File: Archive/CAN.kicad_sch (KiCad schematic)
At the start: 18 parts, among them U3 ISO1044BD, U4 UCC12050DVE

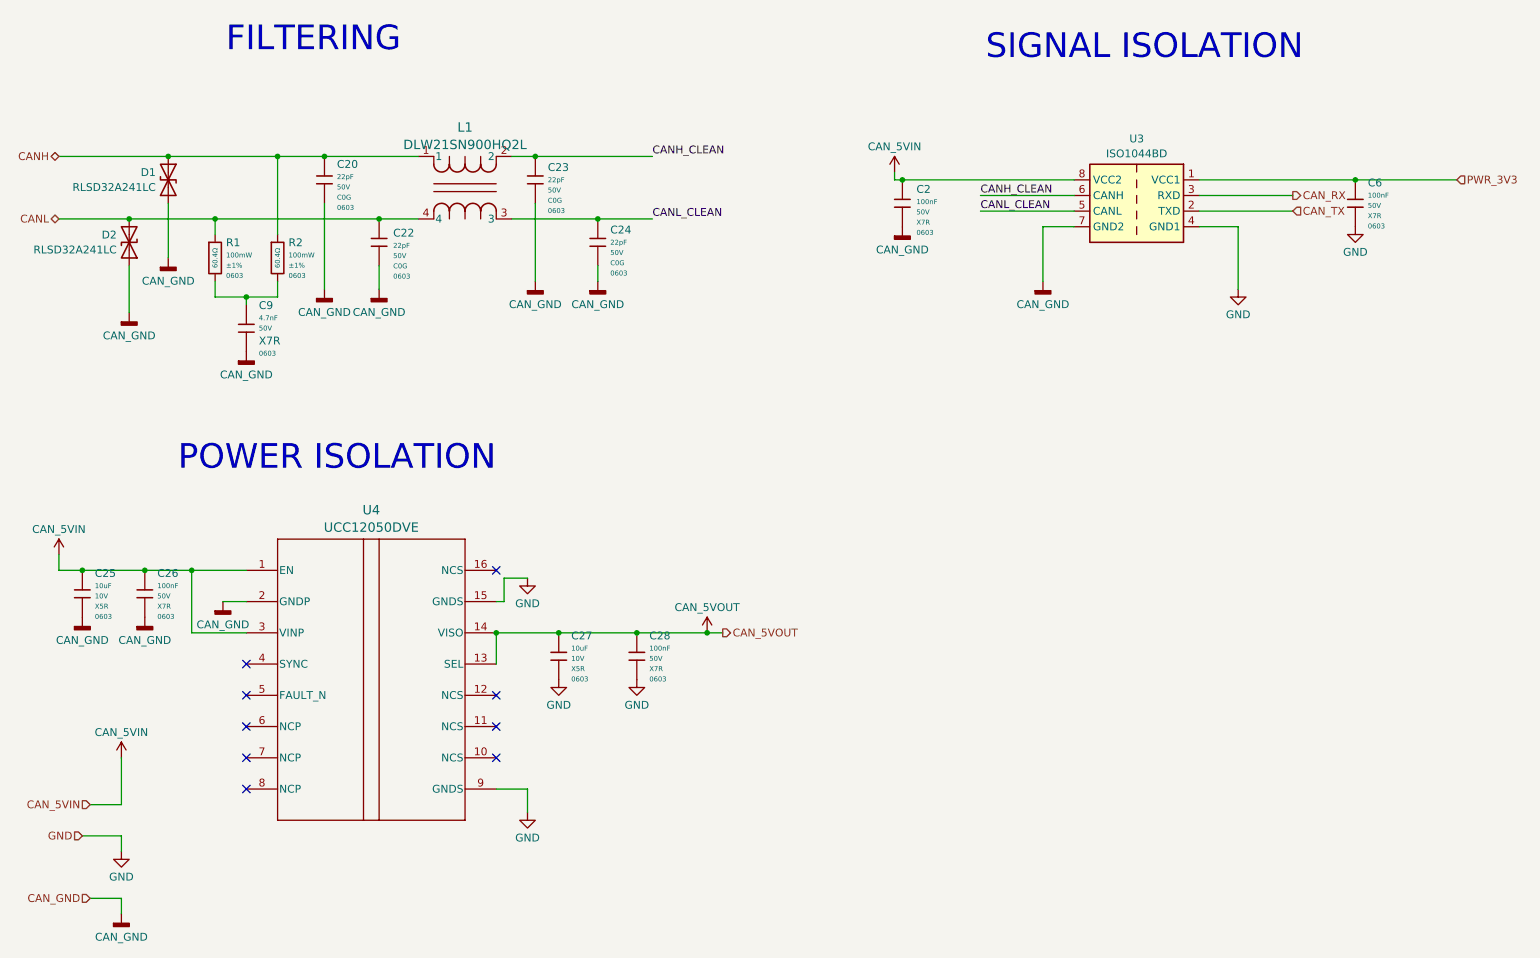
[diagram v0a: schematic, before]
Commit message: Switched to Altium, completed and ordered design
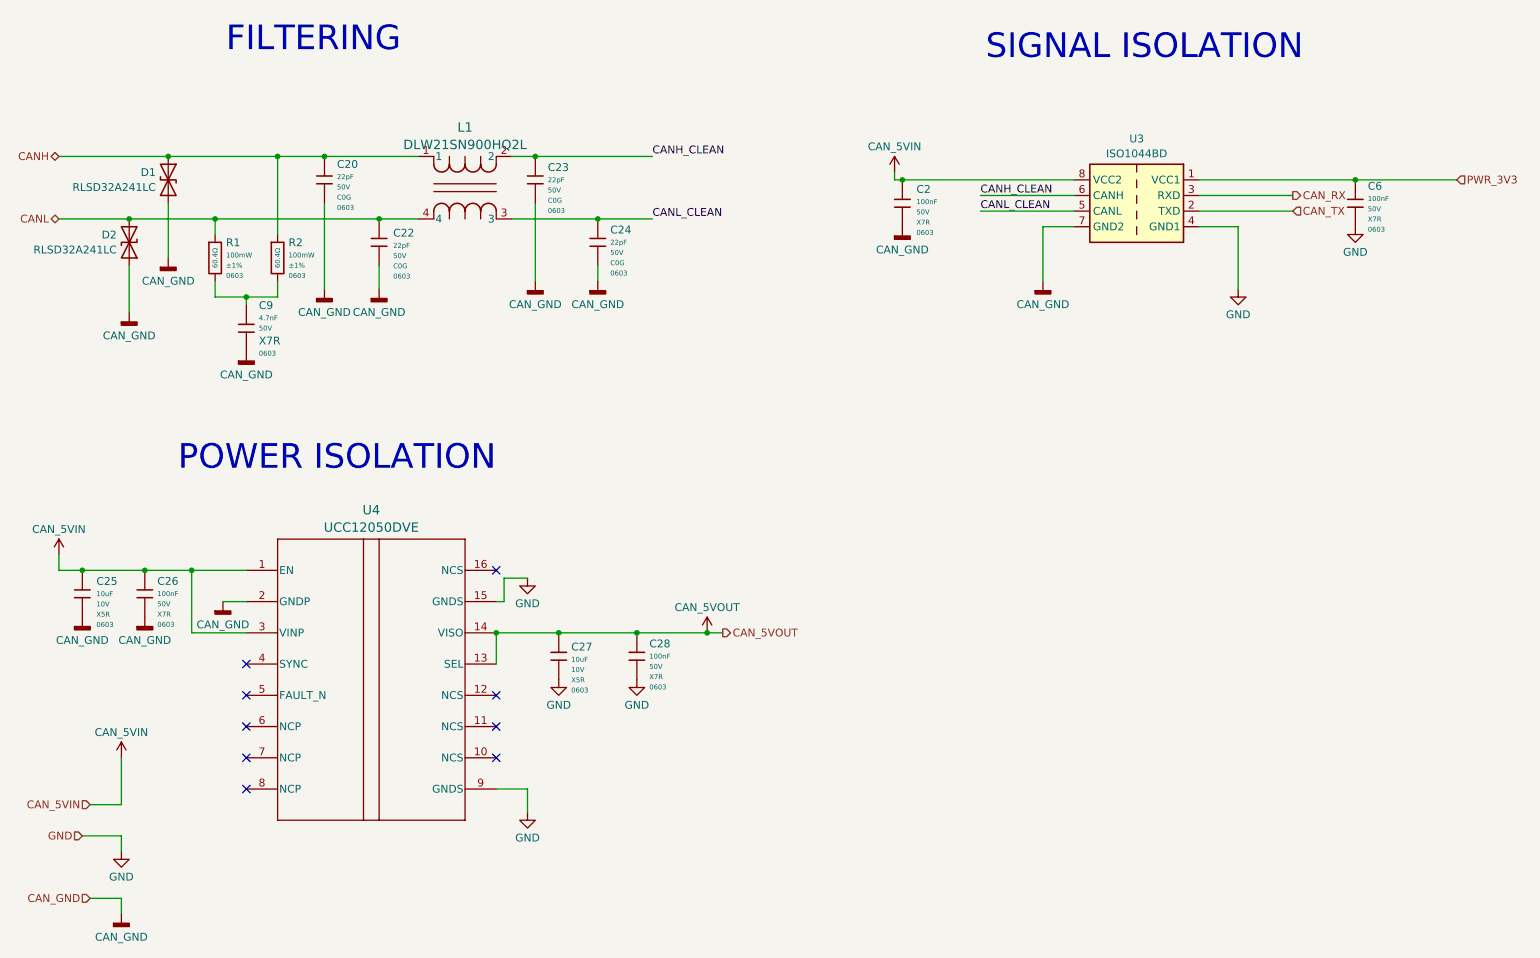
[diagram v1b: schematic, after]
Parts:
- D1, D2: footprint (none) -> PCM_JLCPCB:D_SOD-323
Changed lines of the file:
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@@
 		(on_board yes)
 		(dnp no)
-		(fields_autoplaced yes)
 		(property "Reference" "C25"
-			(at 47.752 127.474 0)
+			(at 48.006 128.778 0)
 			(effects
 				(font
@@
 		)
 		(property "Value" "10uF"
-			(at 47.752 129.5202 0)
+			(at 48.006 130.8242 0)
 			(effects
 				(font
@@
 		)
 		(property "Voltage Rated" "10V"
-			(at 47.752 131.1882 0)
+			(at 48.006 132.4922 0)
 			(effects
 				(font
@@
 		)
 		(property "Temperature Coefficient" "X5R"
-			(at 47.752 132.8562 0)
+			(at 48.006 134.1602 0)
 			(effects
 				(font
@@
 		)
 		(property "Package" "0603"
-			(at 47.752 134.5242 0)
+			(at 48.006 135.8282 0)
 			(effects
 				(font
@@
 		(on_board yes)
 		(dnp no)
-		(fields_autoplaced yes)
 		(property "Reference" "C28"
-			(at 137.922 137.634 0)
+			(at 137.922 138.938 0)
 			(effects
 				(font
@@
 		)
 		(property "Value" "100nF"
-			(at 137.922 139.6802 0)
+			(at 137.922 140.9842 0)
 			(effects
 				(font
@@
 		)
 		(property "Voltage Rated" "50V"
-			(at 137.922 141.3482 0)
+			(at 137.922 142.6522 0)
 			(effects
 				(font
@@
 		)
 		(property "Temperature Coefficient" "X7R"
-			(at 137.922 143.0162 0)
+			(at 137.922 144.3202 0)
 			(effects
 				(font
@@
 		)
 		(property "Package" "0603"
-			(at 137.922 144.6842 0)
+			(at 137.922 145.9882 0)
 			(effects
 				(font
@@
 			)
 		)
-		(property "Footprint" ""
+		(property "Footprint" "PCM_JLCPCB:D_SOD-323"
 			(at 59.69 63.5 0)
 			(effects
@@
 		(on_board yes)
 		(dnp no)
-		(fields_autoplaced yes)
 		(property "Reference" "C6"
-			(at 254.762 63.974 0)
+			(at 254.762 64.516 0)
 			(effects
 				(font
@@
 		)
 		(property "Value" "100nF"
-			(at 254.762 66.0202 0)
+			(at 254.762 66.5622 0)
 			(effects
 				(font
@@
 		)
 		(property "Voltage Rated" "50V"
-			(at 254.762 67.6882 0)
+			(at 254.762 68.2302 0)
 			(effects
 				(font
@@
 		)
 		(property "Temperature Coefficient" "X7R"
-			(at 254.762 69.3562 0)
+			(at 254.762 69.8982 0)
 			(effects
 				(font
@@
 		)
 		(property "Package" "0603"
-			(at 254.762 71.0242 0)
+			(at 254.762 71.5662 0)
 			(effects
 				(font
@@
 		(on_board yes)
 		(dnp no)
-		(fields_autoplaced yes)
 		(property "Reference" "C26"
-			(at 57.912 127.474 0)
+			(at 57.912 128.7638 0)
 			(effects
 				(font
@@
 		)
 		(property "Value" "100nF"
-			(at 57.912 129.5202 0)
+			(at 57.912 130.81 0)
 			(effects
 				(font
@@
 		)
 		(property "Voltage Rated" "50V"
-			(at 57.912 131.1882 0)
+			(at 57.912 132.478 0)
 			(effects
 				(font
@@
 		)
 		(property "Temperature Coefficient" "X7R"
-			(at 57.912 132.8562 0)
+			(at 57.912 134.146 0)
 			(effects
 				(font
@@
 		)
 		(property "Package" "0603"
-			(at 57.912 134.5242 0)
+			(at 57.912 135.814 0)
 			(effects
 				(font
@@
 			)
 		)
-		(property "Footprint" ""
+		(property "Footprint" "PCM_JLCPCB:D_SOD-323"
 			(at 53.34 73.66 0)
 			(effects
@@
 		(on_board yes)
 		(dnp no)
-		(fields_autoplaced yes)
 		(property "Reference" "C27"
-			(at 125.222 137.634 0)
+			(at 125.222 139.446 0)
 			(effects
 				(font
@@
 		)
 		(property "Value" "10uF"
-			(at 125.222 139.6802 0)
+			(at 125.222 141.4922 0)
 			(effects
 				(font
@@
 		)
 		(property "Voltage Rated" "10V"
-			(at 125.222 141.3482 0)
+			(at 125.222 143.1602 0)
 			(effects
 				(font
@@
 		)
 		(property "Temperature Coefficient" "X5R"
-			(at 125.222 143.0162 0)
+			(at 125.222 144.8282 0)
 			(effects
 				(font
@@
 		)
 		(property "Package" "0603"
-			(at 125.222 144.6842 0)
+			(at 125.222 146.4962 0)
 			(effects
 				(font
